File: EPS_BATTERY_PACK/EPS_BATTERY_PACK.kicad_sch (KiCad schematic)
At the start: 47 parts, among them J6001 PT_1000, J6002 HEATER, J6003 HEATER, J6004 Battery, Q6001 NVTFWS4D9N04XMTAG, Q6002 NVTFWS4D9N04XMTAG, U6001 BQ76920PW

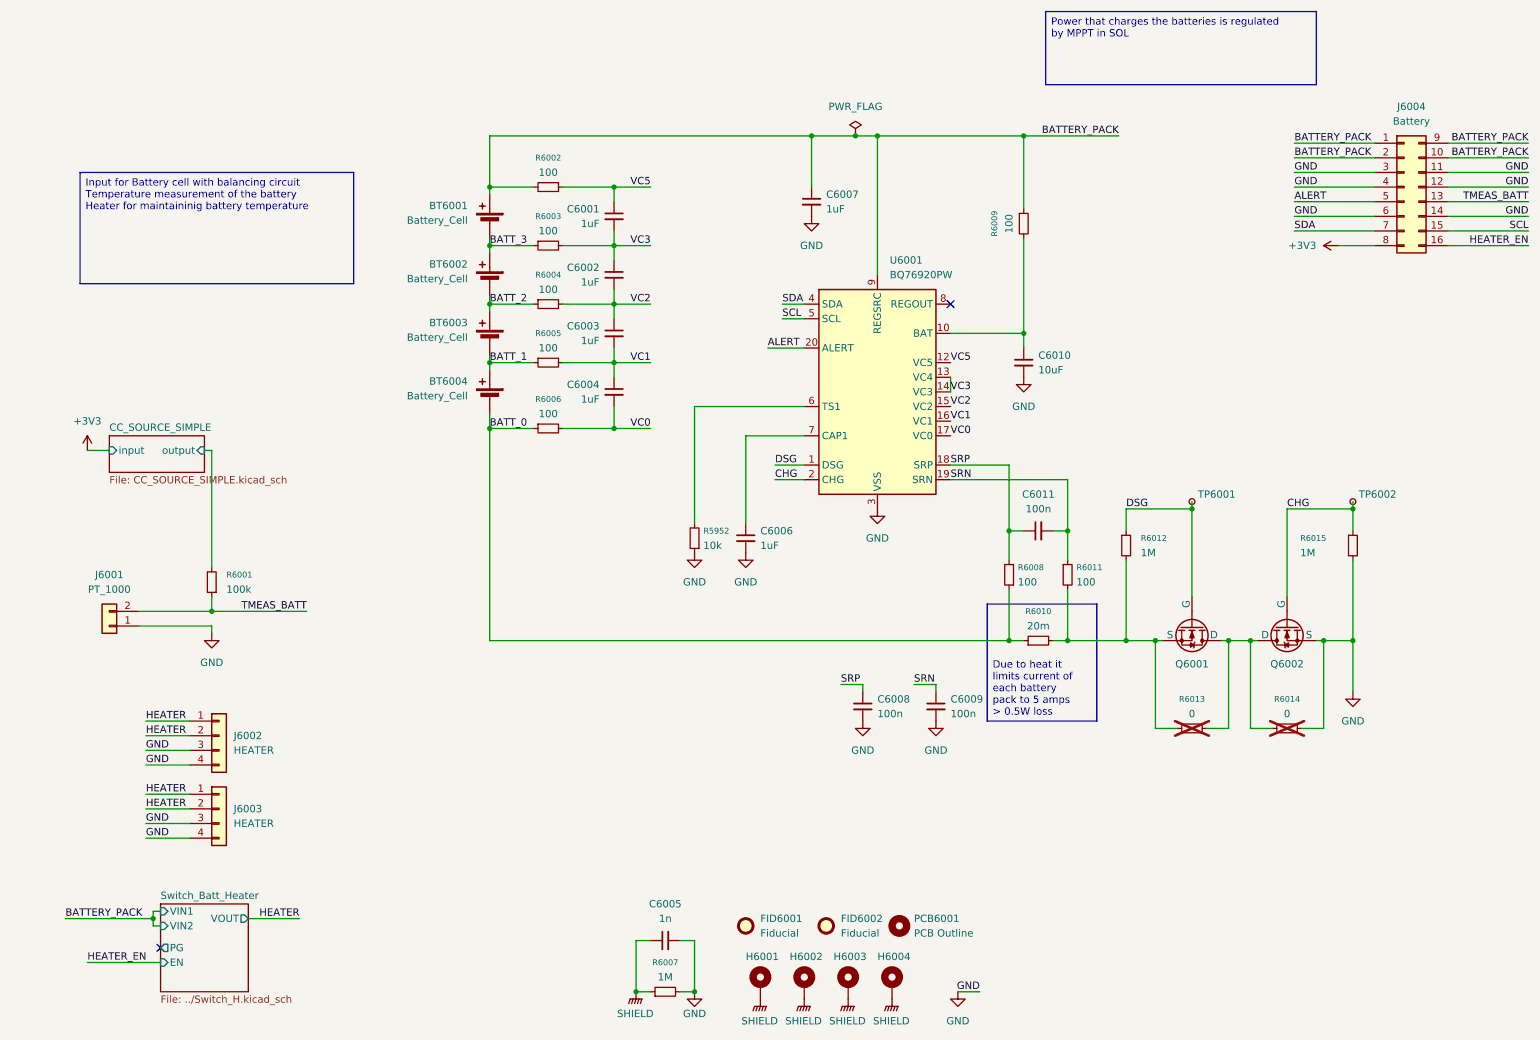
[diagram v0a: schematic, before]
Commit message: added universal switch, added simples current source, reworked test schematic and pcb
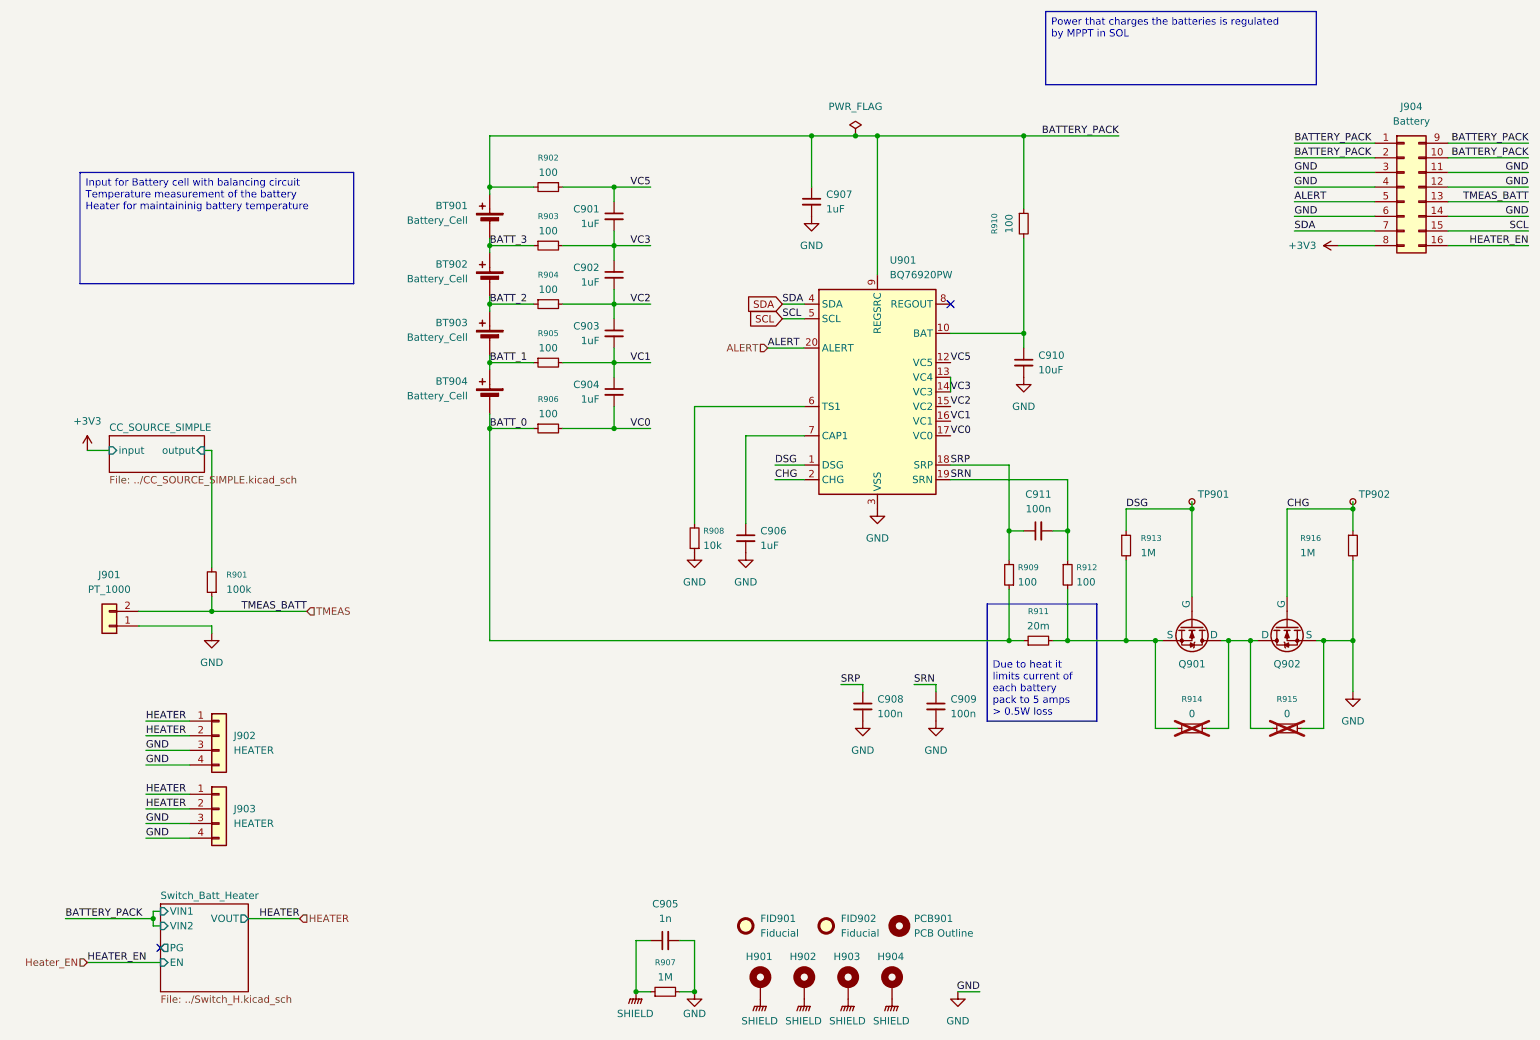
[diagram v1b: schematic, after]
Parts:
- renumbered BT6001 to BT901, BT6002 to BT902, BT6003 to BT903, BT6004 to BT904, C6001 to C901, C6002 to C902, C6003 to C903, C6004 to C904, C6005 to C905, C6006 to C906, C6007 to C907, C6008 to C908, C6009 to C909, C6010 to C910, C6011 to C911, FID6001 to FID901, FID6002 to FID902, H6001 to H901, H6002 to H902, H6003 to H903, H6004 to H904, J6001 to J901, J6002 to J902, J6003 to J903, J6004 to J904, PCB6001 to PCB901, Q6001 to Q901, Q6002 to Q902, R6001 to R901, R6002 to R902, R6003 to R903, R6004 to R904, R6005 to R905, R6006 to R906, R6007 to R907, R5952 to R908, R6008 to R909, R6009 to R910, R6010 to R911, R6011 to R912, R6012 to R913, R6013 to R914, R6014 to R915, R6015 to R916, TP6001 to TP901, TP6002 to TP902, U6001 to U901
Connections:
- net HEATER_EN renamed Heater_EN
- net TMEAS_BATT renamed TMEAS
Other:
- sheet CC_SOURCE_SIMPLE: file CC_SOURCE_SIMPLE.kicad_sch -> ../CC_SOURCE_SIMPLE.kicad_sch

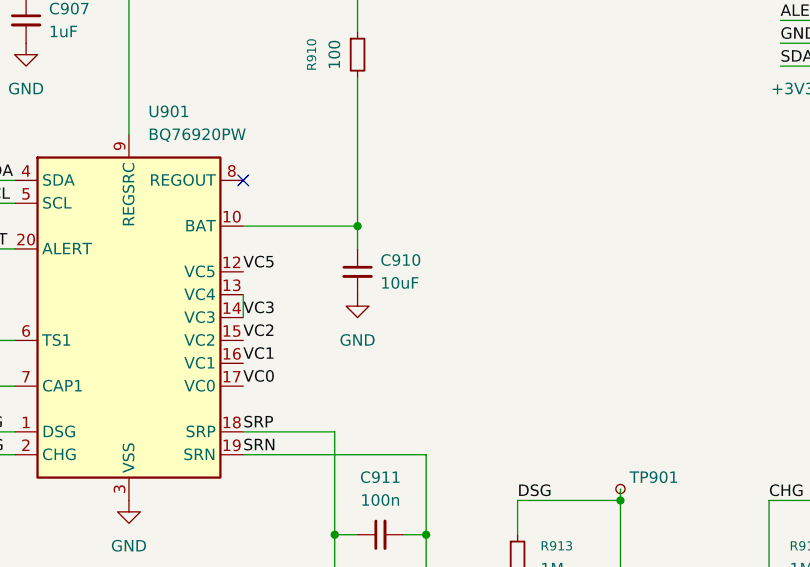
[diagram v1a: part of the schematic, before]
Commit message: Minor changes to acomodate jlcpcb guidelines, this version ordered
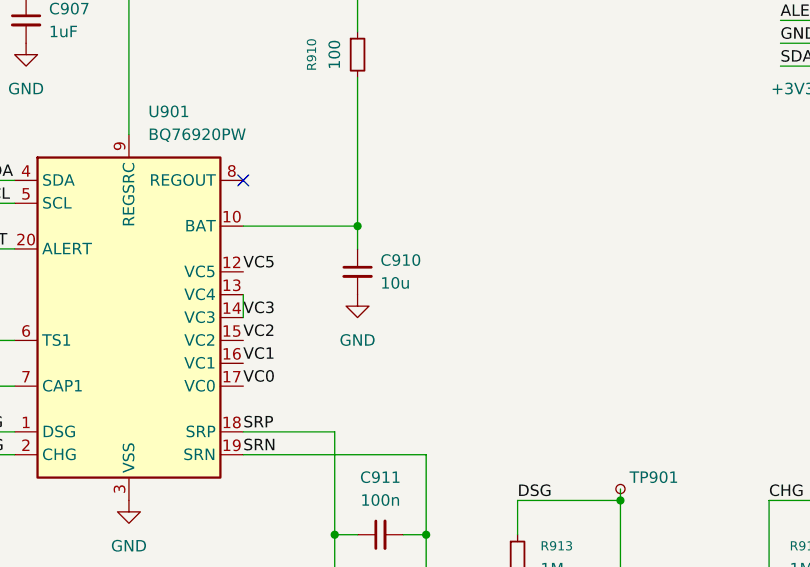
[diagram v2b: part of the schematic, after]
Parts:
- C910: value 10uF -> 10u; footprint Capacitor_SMD:C_0603_1608Metric_Pad1.08x0.95mm_HandSolder -> Capacitor_SMD:C_1206_3216Metric_Pad1.33x1.80mm_HandSolder

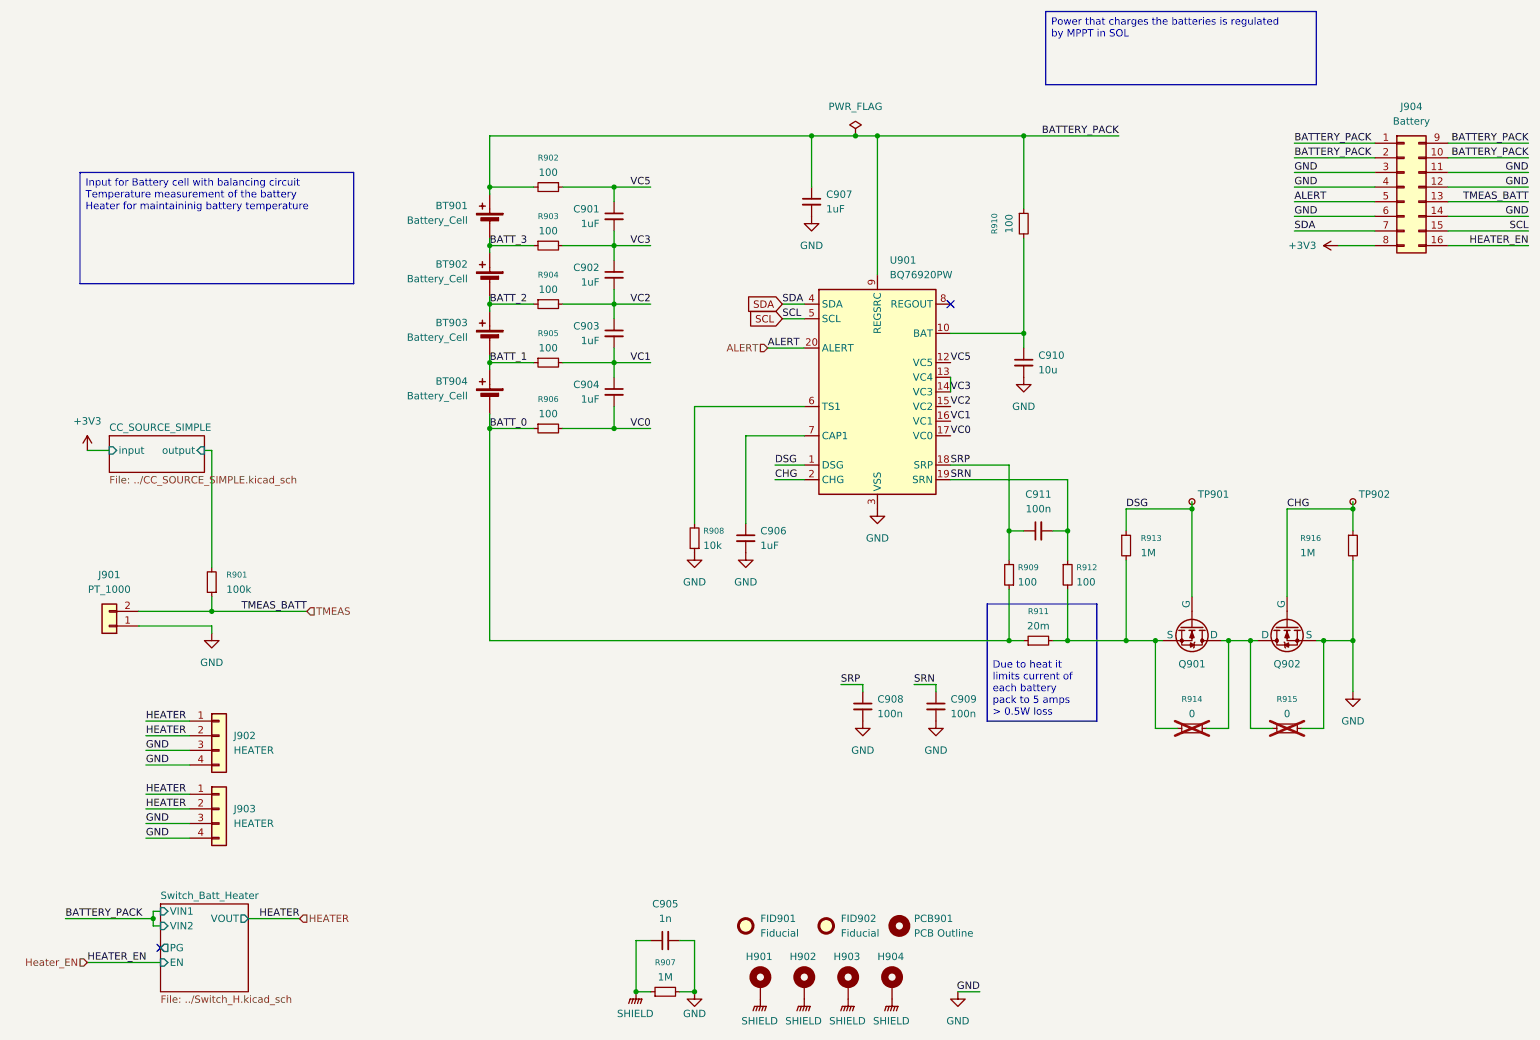
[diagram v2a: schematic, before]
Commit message: changes based on test board manufacturing, mostly added voltage dividers
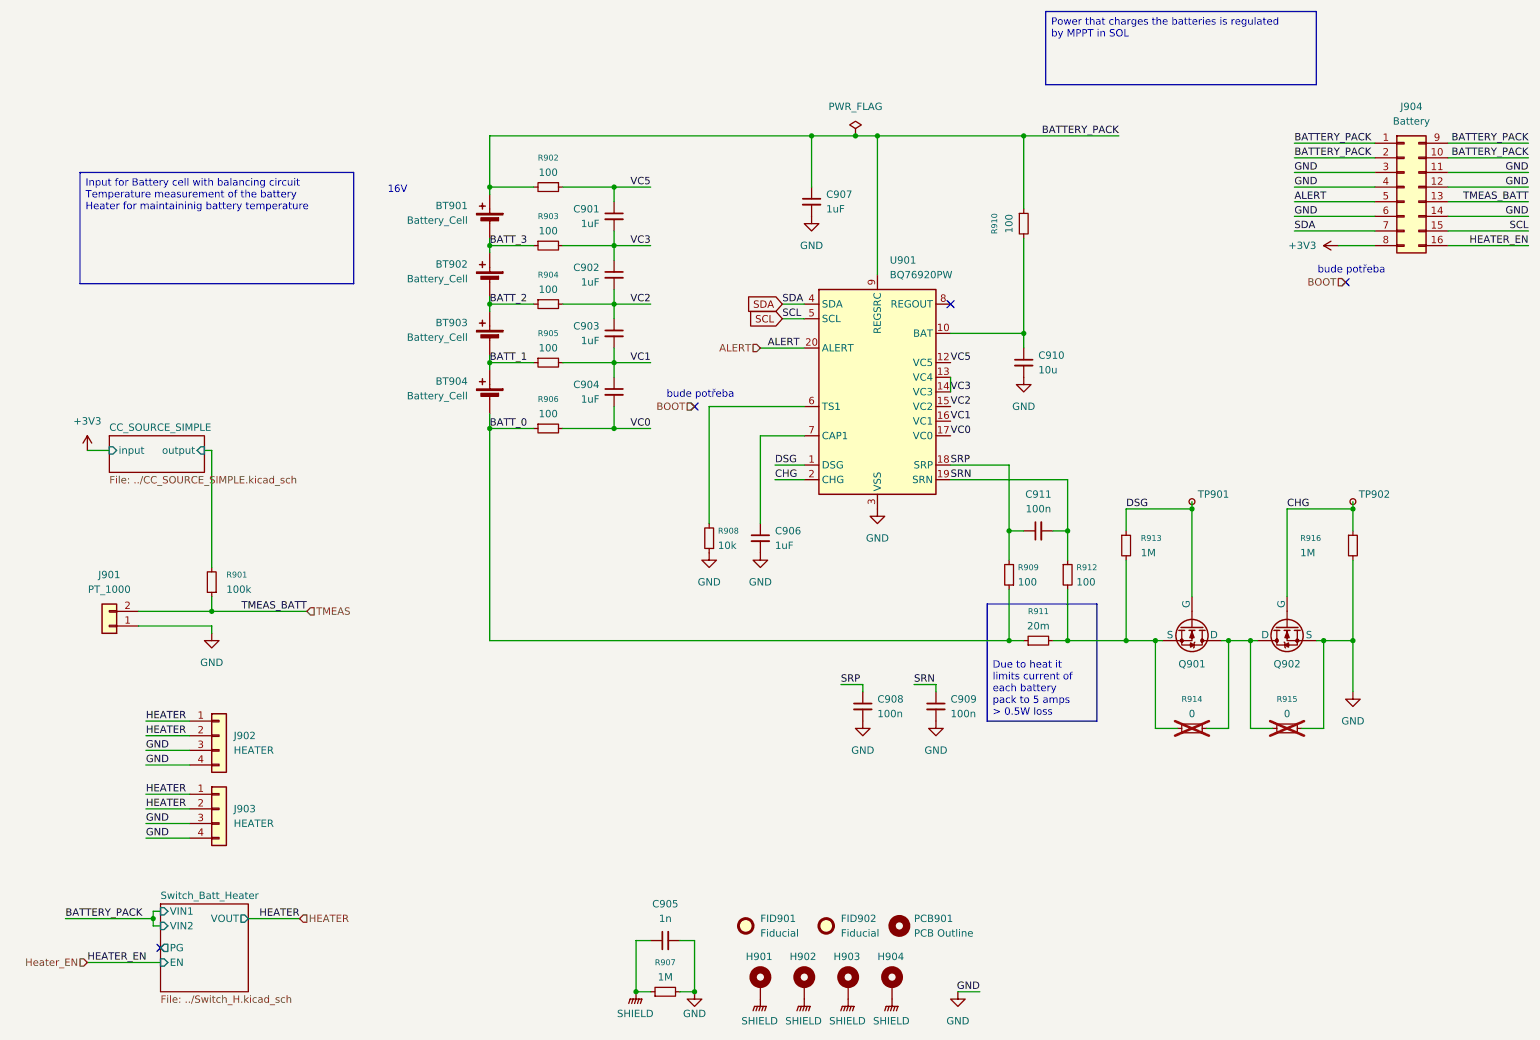
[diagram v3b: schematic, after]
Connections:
- no-connect marks 2 -> 4
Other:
- note added: "16V"
- note added: "bude potřeba"
- moved on the sheet: C906, R908
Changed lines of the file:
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@@
 	(generator_version "9.0")
 	(paper "A4")
+	(text "bude potřeba"
+		(exclude_from_sim no)
+		(at 238.506 61.468 0)
+		(effects
+			(font
+				(size 1.27 1.27)
+				(color 255 0 62 1)
+			)
+		)
+	)
+	(text "bude potřeba"
+		(exclude_from_sim no)
+		(at 125.476 83.058 0)
+		(effects
+			(font
+				(size 1.27 1.27)
+				(color 255 0 62 1)
+			)
+		)
+	)
+	(text "16V"
+		(exclude_from_sim no)
+		(at 72.898 47.498 0)
+		(effects
+			(font
+				(size 1.27 1.27)
+			)
+		)
+	)
 	(text_box "Power that charges the batteries is regulated by MPPT in SOL"
 		(exclude_from_sim no)
@@
 	)
 	(no_connect
+		(at 124.46 85.09)
+	)
+	(no_connect
+		(at 237.49 63.5)
+	)
+	(no_connect
 		(at 31.75 179.07)
 	)
@@
 	(wire
 		(pts
-			(xy 124.46 85.09) (xy 143.51 85.09)
-		)
-		(stroke
-			(width 0)
-			(type default)
-		)
-	)
-	(wire
-		(pts
 			(xy 186.69 106.68) (xy 189.23 106.68)
 		)
@@
 	(wire
 		(pts
-			(xy 133.35 90.17) (xy 143.51 90.17)
+			(xy 135.89 90.17) (xy 143.51 90.17)
 		)
 		(stroke
@@
 	(wire
 		(pts
-			(xy 137.16 74.93) (xy 143.51 74.93)
+			(xy 135.89 74.93) (xy 143.51 74.93)
 		)
 		(stroke
@@
 	(wire
 		(pts
+			(xy 127 85.09) (xy 127 105.41)
+		)
+		(stroke
+			(width 0)
+			(type default)
+		)
+	)
+	(wire
+		(pts
 			(xy 228.6 54.61) (xy 242.57 54.61)
 		)
@@
 	(wire
 		(pts
-			(xy 133.35 90.17) (xy 133.35 105.41)
+			(xy 135.89 90.17) (xy 135.89 105.41)
 		)
 		(stroke
@@
 	(wire
 		(pts
-			(xy 124.46 85.09) (xy 124.46 105.41)
+			(xy 40.64 123.19) (xy 40.64 124.46)
 		)
 		(stroke
@@
 	(wire
 		(pts
-			(xy 40.64 123.19) (xy 40.64 124.46)
+			(xy 228.6 41.91) (xy 242.57 41.91)
 		)
 		(stroke
@@
 	(wire
 		(pts
-			(xy 228.6 41.91) (xy 242.57 41.91)
+			(xy 110.49 57.15) (xy 101.6 57.15)
 		)
 		(stroke
@@
 	(wire
 		(pts
-			(xy 110.49 57.15) (xy 101.6 57.15)
+			(xy 88.9 46.99) (xy 96.52 46.99)
 		)
 		(stroke
@@
 	(wire
 		(pts
-			(xy 88.9 46.99) (xy 96.52 46.99)
+			(xy 255.27 44.45) (xy 269.24 44.45)
 		)
 		(stroke
@@
 	(wire
 		(pts
-			(xy 255.27 44.45) (xy 269.24 44.45)
+			(xy 232.41 125.73) (xy 233.68 125.73)
 		)
 		(stroke
@@
 	(wire
 		(pts
-			(xy 232.41 125.73) (xy 233.68 125.73)
+			(xy 127 85.09) (xy 143.51 85.09)
 		)
 		(stroke
@@
 		)
 	)
+	(hierarchical_label "BOOT"
+		(shape input)
+		(at 124.46 85.09 180)
+		(effects
+			(font
+				(size 1.27 1.27)
+			)
+			(justify right)
+		)
+	)
 	(hierarchical_label "HEATER"
 		(shape input)
@@
 		)
 	)
+	(hierarchical_label "BOOT"
+		(shape input)
+		(at 237.49 63.5 180)
+		(effects
+			(font
+				(size 1.27 1.27)
+			)
+			(justify right)
+		)
+	)
 	(hierarchical_label "ALERT"
 		(shape input)
-		(at 137.16 74.93 180)
+		(at 135.89 74.93 180)
 		(effects
 			(font
@@
 	(symbol
 		(lib_id "Device:C_Small")
-		(at 133.35 107.95 0)
+		(at 135.89 107.95 0)
 		(unit 1)
 		(exclude_from_sim no)
@@
 		(fields_autoplaced yes)
 		(property "Reference" "C906"
-			(at 135.89 106.6862 0)
+			(at 138.43 106.6862 0)
 			(effects
 				(font
@@
 		)
 		(property "Value" "1uF"
-			(at 135.89 109.2262 0)
+			(at 138.43 109.2262 0)
 			(effects
 				(font
@@
 		)
 		(property "Footprint" "Capacitor_SMD:C_0603_1608Metric_Pad1.08x0.95mm_HandSolder"
-			(at 133.35 107.95 0)
+			(at 135.89 107.95 0)
 			(effects
 				(font
@@
 		)
 		(property "Datasheet" "~"
-			(at 133.35 107.95 0)
+			(at 135.89 107.95 0)
 			(effects
 				(font
@@
 		)
 		(property "Description" "Unpolarized capacitor, small symbol"
-			(at 133.35 107.95 0)
+			(at 135.89 107.95 0)
 			(effects
 				(font
@@
 		)
 		(property "CONFIG" ""
-			(at 133.35 107.95 0)
+			(at 135.89 107.95 0)
 			(effects
 				(font
@@
 		)
 		(property "Specification" ""
-			(at 133.35 107.95 0)
+			(at 135.89 107.95 0)
 			(effects
 				(font
@@
 		)
 		(property "mouser_pn" ""
-			(at 133.35 107.95 0)
+			(at 135.89 107.95 0)
 			(effects
 				(font
@@
 	(symbol
 		(lib_id "Device:R_Small")
-		(at 124.46 107.95 180)
+		(at 127 107.95 180)
 		(unit 1)
 		(exclude_from_sim no)
@@
 		(dnp no)
 		(property "Reference" "R908"
-			(at 125.984 106.68 0)
+			(at 128.524 106.68 0)
 			(effects
 				(font
@@
 		)
 		(property "Value" "10k"
-			(at 125.984 109.22 0)
+			(at 128.524 109.22 0)
 			(effects
 				(font
@@
 		)
 		(property "Footprint" "Resistor_SMD:R_0603_1608Metric_Pad0.98x0.95mm_HandSolder"
-			(at 124.46 107.95 0)
+			(at 127 107.95 0)
 			(effects
 				(font
@@
 		)
 		(property "Datasheet" "~"
-			(at 124.46 107.95 0)
+			(at 127 107.95 0)
 			(effects
 				(font
@@
 		)
 		(property "Description" "Resistor, small symbol"
-			(at 124.46 107.95 0)
+			(at 127 107.95 0)
 			(effects
 				(font
@@
 		)
 		(property "CONFIG" ""
-			(at 124.46 107.95 0)
+			(at 127 107.95 0)
 			(effects
 				(font
@@
 		)
 		(property "Specification" ""
-			(at 124.46 107.95 0)
+			(at 127 107.95 0)
 			(effects
 				(font
@@
 		)
 		(property "mouser_pn" ""
-			(at 124.46 107.95 0)
+			(at 127 107.95 0)
 			(effects
 				(font
@@
 	(symbol
 		(lib_id "power:GND")
-		(at 124.46 110.49 0)
+		(at 127 110.49 0)
 		(unit 1)
 		(exclude_from_sim no)
@@
 		(fields_autoplaced yes)
 		(property "Reference" "#PWR0904"
-			(at 124.46 116.84 0)
+			(at 127 116.84 0)
 			(effects
 				(font
@@
 		)
 		(property "Value" "GND"
-			(at 124.46 115.57 0)
+			(at 127 115.57 0)
 			(effects
 				(font
@@
 		)
 		(property "Footprint" ""
-			(at 124.46 110.49 0)
+			(at 127 110.49 0)
 			(effects
 				(font
@@
 		)
 		(property "Datasheet" ""
-			(at 124.46 110.49 0)
+			(at 127 110.49 0)
 			(effects
 				(font
@@
 		)
 		(property "Description" "Power symbol creates a global label with name \"GND\" , ground"
-			(at 124.46 110.49 0)
+			(at 127 110.49 0)
 			(effects
 				(font
@@
 	(symbol
 		(lib_id "power:GND")
-		(at 133.35 110.49 0)
+		(at 135.89 110.49 0)
 		(unit 1)
 		(exclude_from_sim no)
@@
 		(fields_autoplaced yes)
 		(property "Reference" "#PWR0906"
-			(at 133.35 116.84 0)
+			(at 135.89 116.84 0)
 			(effects
 				(font
@@
 		)
 		(property "Value" "GND"
-			(at 133.35 115.57 0)
+			(at 135.89 115.57 0)
 			(effects
 				(font
@@
 		)
 		(property "Footprint" ""
-			(at 133.35 110.49 0)
+			(at 135.89 110.49 0)
 			(effects
 				(font
@@
 		)
 		(property "Datasheet" ""
-			(at 133.35 110.49 0)
+			(at 135.89 110.49 0)
 			(effects
 				(font
@@
 		)
 		(property "Description" "Power symbol creates a global label with name \"GND\" , ground"
-			(at 133.35 110.49 0)
+			(at 135.89 110.49 0)
 			(effects
 				(font

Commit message: nearly finnished CORE pcb
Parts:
- renumbered BT901 to BT6001, BT902 to BT6002, BT903 to BT6003, BT904 to BT6004, C901 to C6001, C902 to C6002, C903 to C6003, C904 to C6004, C905 to C6005, C906 to C6006, C907 to C6007, C908 to C6008, C909 to C6009, C910 to C6010, C911 to C6011, FID901 to FID6001, FID902 to FID6002, H901 to H6001, H902 to H6002, H903 to H6003, H904 to H6004, J901 to J6001, J902 to J6002, J903 to J6003, J904 to J6004, PCB901 to PCB6001, Q901 to Q6001, Q902 to Q6002, R908 to R5952, R901 to R6001, R902 to R6002, R903 to R6003, R904 to R6004, R905 to R6005, R906 to R6006, R907 to R6007, R909 to R6008, R910 to R6009, R911 to R6010, R912 to R6011, R913 to R6012, R914 to R6013, R915 to R6014, R916 to R6015, TP901 to TP6001, TP902 to TP6002, U901 to U6001
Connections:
- net +3V3 is gone; now on net BOOT: J6004.8 (Pin_8)
- net +2.5V: now reaches U6001.8 (REGOUT)
- no-connect marks 4 -> 2
